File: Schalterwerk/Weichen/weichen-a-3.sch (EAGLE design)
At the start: 24 parts, among them Q1 P-MOSFET, Q2 P-MOSFET, X1 PHNX_4P_508CONN_1017493, X3 IO-HAT, X4 RJ45-JACK, X5 PHNX_4P_350CONN_1984989_PXC, X6 PHNX_4P_350CONN_1984989_PXC

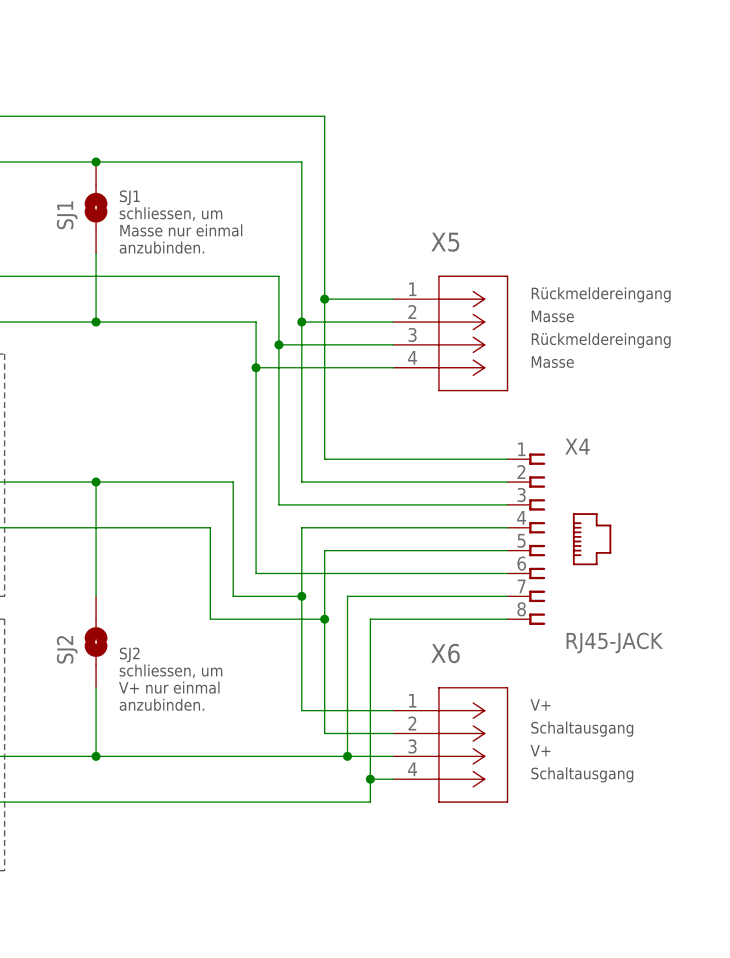
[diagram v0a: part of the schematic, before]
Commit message: Completes copy-paste of the layout of the conneectors to the schalterwerk.
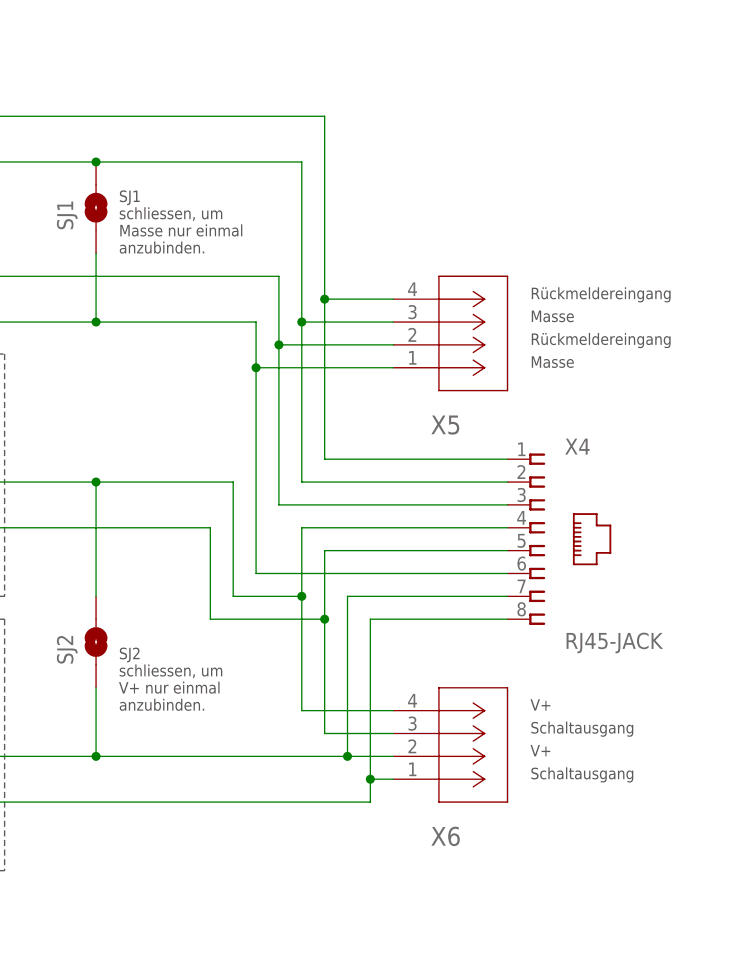
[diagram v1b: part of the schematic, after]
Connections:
- net NX41: now also X5.4; no longer X5.1
- net NX42: now also X5.3; no longer X5.2
- net NX43: now also X5.2; no longer X5.3
- net NX44: now also X6.4; no longer X6.1
- net NX45: now also X6.3; no longer X6.2
- net NX46: now also X5.1; no longer X5.4
- net NX47: now also X6.2; no longer X6.3
- net NX48: now also X6.1; no longer X6.4
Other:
- moved on the sheet: X5, X6
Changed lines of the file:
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@@
 <attribute name="VALUE" x="234.95" y="72.898" size="1.778" layer="96"/>
 </instance>
-<instance part="X5" gate="A" x="215.9" y="111.76" smashed="yes">
-<attribute name="NAME" x="220.0646" y="117.0686" size="2.083" layer="95" ratio="6"/>
-</instance>
-<instance part="X6" gate="A" x="215.9" y="66.04" smashed="yes">
-<attribute name="NAME" x="220.0646" y="71.3486" size="2.083" layer="95" ratio="6"/>
+<instance part="X5" gate="A" x="215.9" y="104.14" smashed="yes" rot="MR180">
+<attribute name="NAME" x="220.0646" y="98.8314" size="2.083" layer="95" ratio="6" rot="MR180"/>
+</instance>
+<instance part="X6" gate="A" x="215.9" y="58.42" smashed="yes" rot="MR180">
+<attribute name="NAME" x="220.0646" y="53.1114" size="2.083" layer="95" ratio="6" rot="MR180"/>
 </instance>
 <instance part="OK2" gate="A" x="139.7" y="129.54" smashed="yes">
@@
 <wire x1="208.28" y1="132.08" x2="208.28" y2="111.76" width="0.1524" layer="91"/>
 <pinref part="X4" gate="G$1" pin="1"/>
+<wire x1="208.28" y1="111.76" x2="208.28" y2="93.98" width="0.1524" layer="91"/>
 <wire x1="228.6" y1="93.98" x2="208.28" y2="93.98" width="0.1524" layer="91"/>
-<wire x1="208.28" y1="93.98" x2="208.28" y2="111.76" width="0.1524" layer="91"/>
-<junction x="208.28" y="111.76"/>
-<pinref part="X5" gate="A" pin="1"/>
-<wire x1="208.28" y1="111.76" x2="215.9" y2="111.76" width="0.1524" layer="91"/>
 <pinref part="R11" gate="G$1" pin="1"/>
 <wire x1="208.28" y1="132.08" x2="160.02" y2="132.08" width="0.1524" layer="91"/>
+<pinref part="X5" gate="A" pin="4"/>
+<wire x1="208.28" y1="111.76" x2="215.9" y2="111.76" width="0.1524" layer="91"/>
+<junction x="208.28" y="111.76"/>
 </segment>
 </net>
 <net name="NX42" class="0">
 <segment>
-<wire x1="205.74" y1="127" x2="205.74" y2="109.22" width="0.1524" layer="91"/>
-<wire x1="205.74" y1="109.22" x2="215.9" y2="109.22" width="0.1524" layer="91"/>
 <pinref part="X4" gate="G$1" pin="2"/>
 <wire x1="228.6" y1="91.44" x2="205.74" y2="91.44" width="0.1524" layer="91"/>
 <wire x1="205.74" y1="91.44" x2="205.74" y2="109.22" width="0.1524" layer="91"/>
-<junction x="205.74" y="109.22"/>
-<pinref part="X5" gate="A" pin="2"/>
 <pinref part="OK2" gate="A" pin="EMIT"/>
+<wire x1="205.74" y1="109.22" x2="205.74" y2="127" width="0.1524" layer="91"/>
 <wire x1="147.32" y1="127" x2="182.88" y2="127" width="0.1524" layer="91"/>
 <pinref part="SJ1" gate="1" pin="2"/>
 <wire x1="182.88" y1="127" x2="205.74" y2="127" width="0.1524" layer="91"/>
 <junction x="182.88" y="127"/>
+<pinref part="X5" gate="A" pin="3"/>
+<wire x1="205.74" y1="109.22" x2="215.9" y2="109.22" width="0.1524" layer="91"/>
+<junction x="205.74" y="109.22"/>
 </segment>
 </net>
 <net name="NX43" class="0">
 <segment>
-<wire x1="203.2" y1="114.3" x2="203.2" y2="106.68" width="0.1524" layer="91"/>
-<wire x1="203.2" y1="106.68" x2="215.9" y2="106.68" width="0.1524" layer="91"/>
-<pinref part="X5" gate="A" pin="3"/>
 <pinref part="R12" gate="G$1" pin="1"/>
 <wire x1="203.2" y1="114.3" x2="160.02" y2="114.3" width="0.1524" layer="91"/>
 <pinref part="X4" gate="G$1" pin="3"/>
 <wire x1="228.6" y1="88.9" x2="203.2" y2="88.9" width="0.1524" layer="91"/>
+<wire x1="203.2" y1="114.3" x2="203.2" y2="106.68" width="0.1524" layer="91"/>
+<pinref part="X5" gate="A" pin="2"/>
 <wire x1="203.2" y1="106.68" x2="203.2" y2="88.9" width="0.1524" layer="91"/>
+<wire x1="203.2" y1="106.68" x2="215.9" y2="106.68" width="0.1524" layer="91"/>
 <junction x="203.2" y="106.68"/>
 </segment>
@@
 <wire x1="208.28" y1="76.2" x2="208.28" y2="63.5" width="0.1524" layer="91"/>
 <junction x="208.28" y="76.2"/>
-<pinref part="X6" gate="A" pin="2"/>
-<wire x1="208.28" y1="63.5" x2="215.9" y2="63.5" width="0.1524" layer="91"/>
 <pinref part="OK2" gate="C" pin="C"/>
 <wire x1="144.78" y1="86.36" x2="195.58" y2="86.36" width="0.1524" layer="91"/>
 <wire x1="195.58" y1="86.36" x2="195.58" y2="76.2" width="0.1524" layer="91"/>
 <wire x1="195.58" y1="76.2" x2="208.28" y2="76.2" width="0.1524" layer="91"/>
+<pinref part="X6" gate="A" pin="3"/>
+<wire x1="208.28" y1="63.5" x2="215.9" y2="63.5" width="0.1524" layer="91"/>
 </segment>
 </net>
 <net name="NX46" class="0">
 <segment>
-<wire x1="200.66" y1="109.22" x2="200.66" y2="104.14" width="0.1524" layer="91"/>
-<wire x1="200.66" y1="104.14" x2="215.9" y2="104.14" width="0.1524" layer="91"/>
-<pinref part="X5" gate="A" pin="4"/>
 <pinref part="OK2" gate="B" pin="EMIT"/>
 <wire x1="200.66" y1="109.22" x2="182.88" y2="109.22" width="0.1524" layer="91"/>
@@
 <pinref part="X4" gate="G$1" pin="6"/>
 <wire x1="200.66" y1="81.28" x2="228.6" y2="81.28" width="0.1524" layer="91"/>
+<wire x1="200.66" y1="109.22" x2="200.66" y2="104.14" width="0.1524" layer="91"/>
+<pinref part="X5" gate="A" pin="1"/>
 <wire x1="200.66" y1="104.14" x2="200.66" y2="81.28" width="0.1524" layer="91"/>
+<wire x1="200.66" y1="104.14" x2="215.9" y2="104.14" width="0.1524" layer="91"/>
 <junction x="200.66" y="104.14"/>
 </segment>
@@
 <wire x1="205.74" y1="86.36" x2="205.74" y2="78.74" width="0.1524" layer="91"/>
 <wire x1="205.74" y1="78.74" x2="205.74" y2="66.04" width="0.1524" layer="91"/>
-<wire x1="205.74" y1="66.04" x2="215.9" y2="66.04" width="0.1524" layer="91"/>
 <junction x="205.74" y="78.74"/>
-<pinref part="X6" gate="A" pin="1"/>
 <pinref part="R13" gate="G$1" pin="1"/>
 <wire x1="205.74" y1="78.74" x2="198.12" y2="78.74" width="0.1524" layer="91"/>
@@
 <wire x1="182.88" y1="78.74" x2="182.88" y2="91.44" width="0.1524" layer="91"/>
 <junction x="182.88" y="91.44"/>
+<pinref part="X6" gate="A" pin="4"/>
+<wire x1="205.74" y1="66.04" x2="215.9" y2="66.04" width="0.1524" layer="91"/>
 </segment>
 </net>
@@
 <wire x1="228.6" y1="78.74" x2="210.82" y2="78.74" width="0.1524" layer="91"/>
 <wire x1="210.82" y1="78.74" x2="210.82" y2="60.96" width="0.1524" layer="91"/>
-<pinref part="X6" gate="A" pin="3"/>
-<wire x1="210.82" y1="60.96" x2="215.9" y2="60.96" width="0.1524" layer="91"/>
-<junction x="210.82" y="60.96"/>
 <wire x1="210.82" y1="60.96" x2="182.88" y2="60.96" width="0.1524" layer="91"/>
 <pinref part="SJ2" gate="1" pin="1"/>
@@
 <wire x1="160.02" y1="60.96" x2="182.88" y2="60.96" width="0.1524" layer="91"/>
 <junction x="182.88" y="60.96"/>
+<pinref part="X6" gate="A" pin="2"/>
+<wire x1="210.82" y1="60.96" x2="215.9" y2="60.96" width="0.1524" layer="91"/>
+<junction x="210.82" y="60.96"/>
 </segment>
 </net>
@@
 <wire x1="228.6" y1="76.2" x2="213.36" y2="76.2" width="0.1524" layer="91"/>
 <wire x1="213.36" y1="76.2" x2="213.36" y2="58.42" width="0.1524" layer="91"/>
-<pinref part="X6" gate="A" pin="4"/>
 <wire x1="213.36" y1="58.42" x2="213.36" y2="55.88" width="0.1524" layer="91"/>
+<wire x1="144.78" y1="55.88" x2="213.36" y2="55.88" width="0.1524" layer="91"/>
+<pinref part="X6" gate="A" pin="1"/>
 <wire x1="213.36" y1="58.42" x2="215.9" y2="58.42" width="0.1524" layer="91"/>
 <junction x="213.36" y="58.42"/>
-<wire x1="144.78" y1="55.88" x2="213.36" y2="55.88" width="0.1524" layer="91"/>
-</segment>
-</net>
+</segment>
+</net>

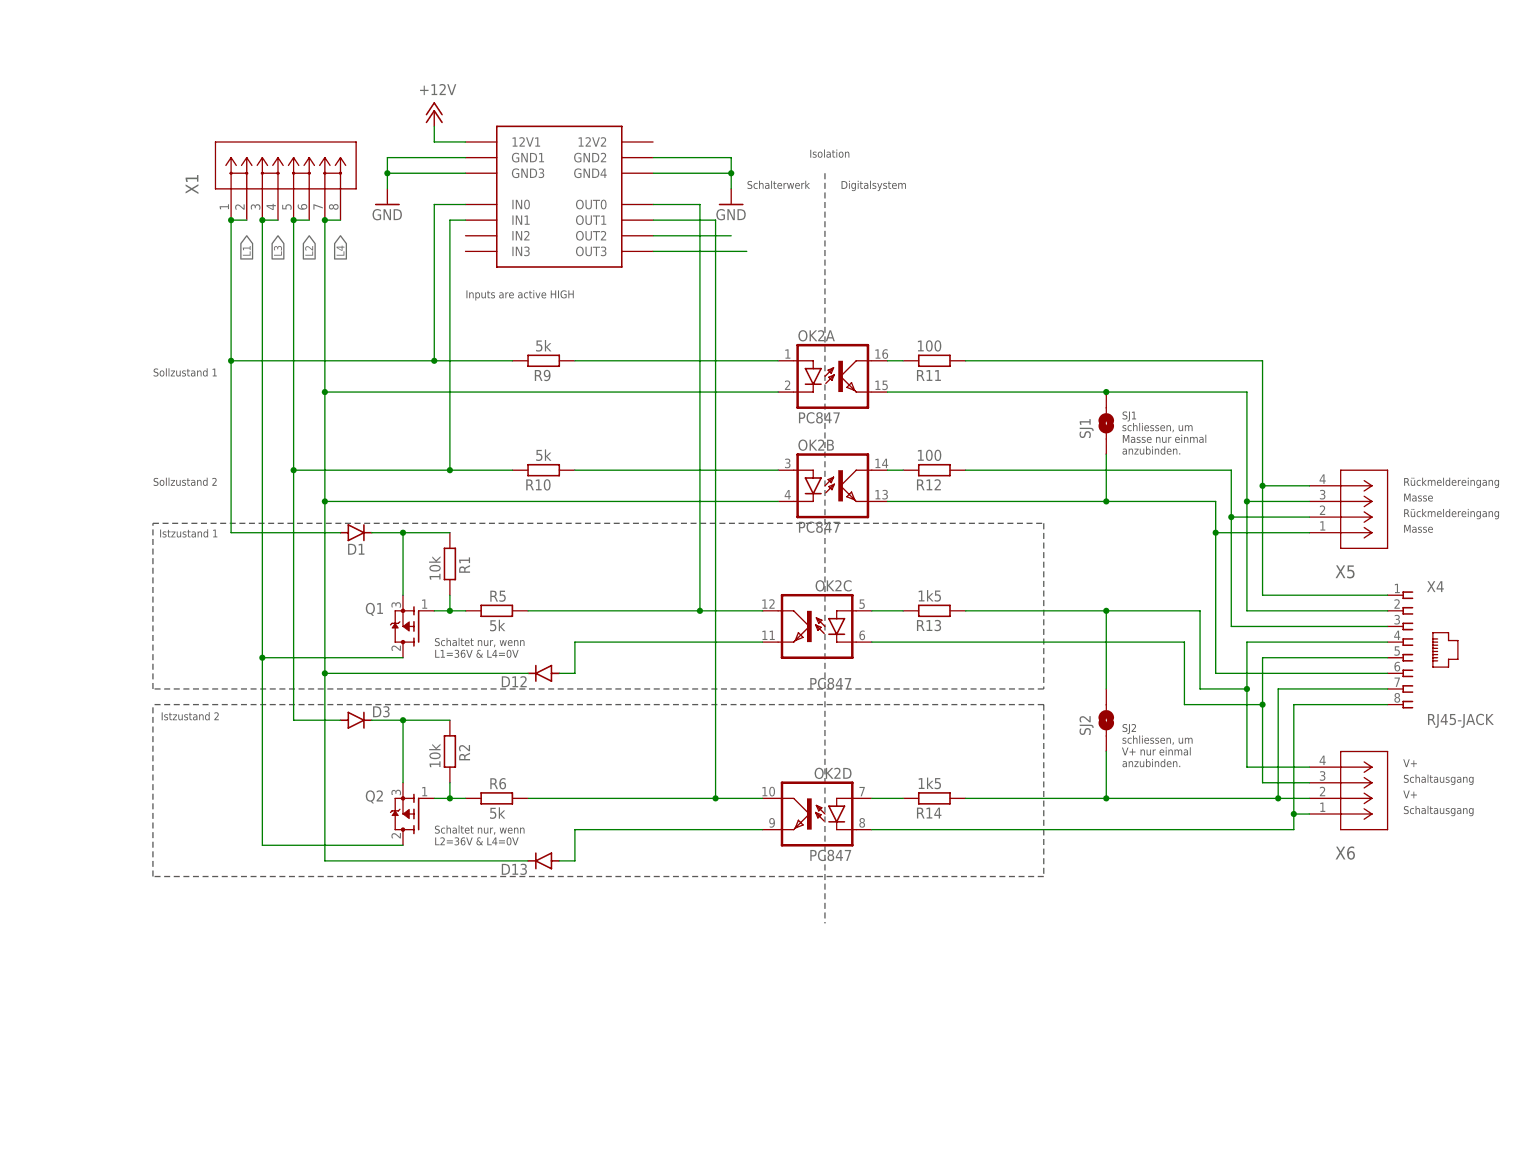
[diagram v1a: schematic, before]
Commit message: Does much of the board layout. Switches the pins on the connector to the schalterwerk so that it is in the order of L1 .. L4.
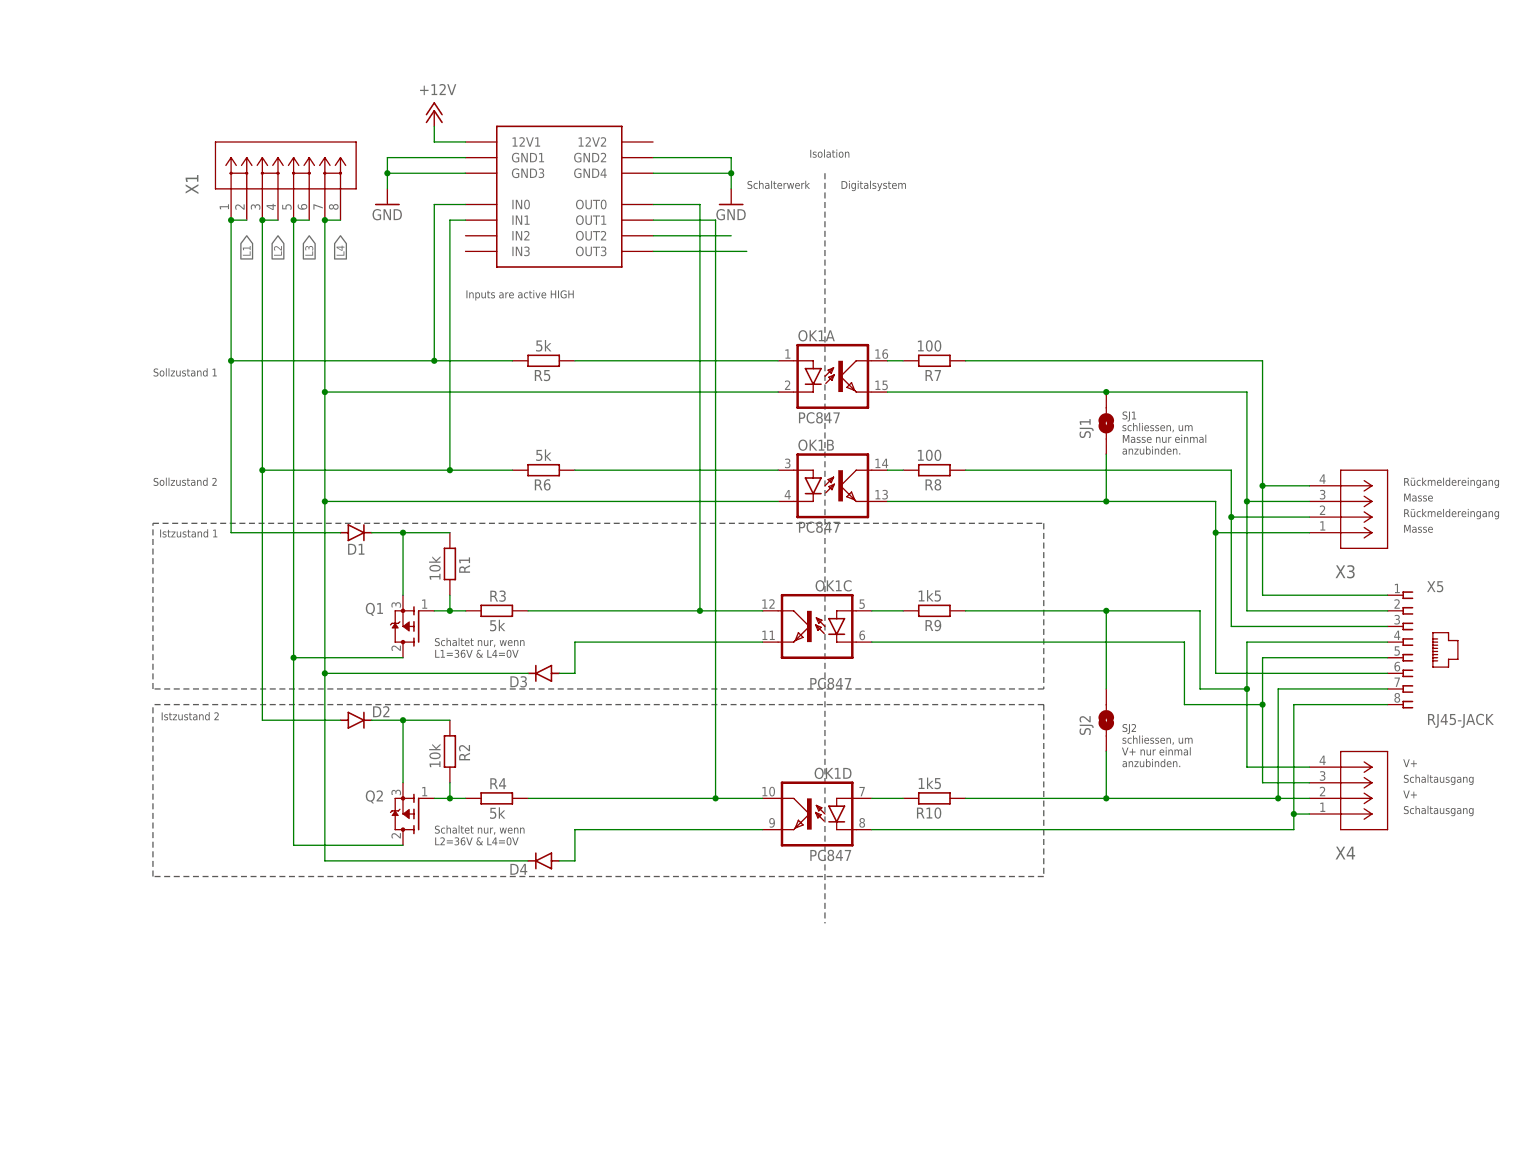
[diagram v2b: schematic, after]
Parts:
- removed D12: (no value), diode:DIODE-MINIMELF
- removed R13, R14: 1k5, rcl:R-EU_R0805
- removed X6: PHNX_4P_350CONN_1984989_PXC, eagleparts:PHNX_4P_350CONN_1984989_PXC
- added D2: (no value), diode:DIODE-DO214AC
- added R3, R4: 5k, rcl:R-EU_R0805
- added X2: IO-HAT, eagleparts:IO-HAT
- D3: device diode:DIODE-DO214AC -> diode:DIODE-MINIMELF
- R10, R9: value 5k -> 1k5
- X3: value IO-HAT -> PHNX_4P_350CONN_1984989_PXC; device eagleparts:IO-HAT -> eagleparts:PHNX_4P_350CONN_1984989_PXC
- X4: value RJ45-JACK -> PHNX_4P_350CONN_1984989_PXC; device trainlib:RJ45-JACKRJ45-PULSE-E5J00 -> eagleparts:PHNX_4P_350CONN_1984989_PXC
- X5: value PHNX_4P_350CONN_1984989_PXC -> RJ45-JACK; device eagleparts:PHNX_4P_350CONN_1984989_PXC -> trainlib:RJ45-JACKRJ45-PULSE-E5J00
- renumbered D13 to D4, OK2 to OK1, R11 to R7, R12 to R8
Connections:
- net +12V: now also X2G$1.12V1; no longer X3G$1.12V1
- net GND: now also X2G$1.GND1, X2G$1.GND2, X2G$1.GND3, X2G$1.GND4; no longer X3G$1.GND1, X3G$1.GND2, X3G$1.GND3, X3G$1.GND4
- net L1: now also R5.2, X2G$1.IN0; no longer R9.2, X3G$1.IN0
- net L2: now also D2.A, R6.2, X1.3, X1.4, X2G$1.IN1; no longer D3.A, R10.2, X1.5, X1.6, X3G$1.IN1
- net L3: now also X1.5, X1.6; no longer X1.3, X1.4
- net L4: now also D3.C; no longer D12.C
- net N$1: now also D2.C; no longer D3.C
- net N$12: now also R4.1; no longer R6.1
- net N$15: now also R3.2, X2G$1.OUT0; no longer R5.2, X3G$1.OUT0
- net N$16: now also R4.2, X2G$1.OUT1; no longer R6.2, X3G$1.OUT1
- net N$17: now also D3.A; no longer D12.A
- net N$2: now also R5.1; no longer R9.1
- net N$24: now also X2G$1.OUT2; no longer X3G$1.OUT2
- net N$25: now also X2G$1.OUT3; no longer X3G$1.OUT3
- net N$5: now also R9.2; no longer R13.2
- net N$7: now also R6.1; no longer R10.1
- net N$8: now also R10.2; no longer R14.2
- net N$9: now also R3.1; no longer R5.1
- net NX41: now also X3.4, X5.1; no longer X4.1, X5.4
- net NX42: now also X3.3, X5.2; no longer X4.2, X5.3
- net NX43: now also X3.2, X5.3; no longer X4.3, X5.2
- net NX44: now also R9.1, X5.4; no longer R13.1, X6.4
- net NX45: now also X4.3, X5.5; no longer X4.5, X6.3
- net NX46: now also X3.1, X5.6; no longer X4.6, X5.1
- net NX47: now also R10.1, X4.2, X5.7; no longer R14.1, X4.7, X6.2
- net NX48: now also X4.1, X5.8; no longer X4.8, X6.1
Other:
- moved on the sheet: D3, R10, R5, R6, R9
